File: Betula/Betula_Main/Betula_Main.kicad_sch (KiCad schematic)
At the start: 172 parts, among them J1 Conn_02x15_Top_Bottom, J2 Conn_02x02_Top_Bottom, J3 Conn_02x15_Top_Bottom, J4 Conn_01x03_Male, J5 Conn_01x03_Male, J6 Conn_02x05_Odd_Even, Q1 FDS4435BZ, Q2 DMN3030LSS, U1 PCM1803A, U10 V1402, U11 74HCT125, U12 TLV9354, U13 TLV9354, U14 TLV9352, U15 TLV9354, U16 TLV9354, U2 PCM1803A, U3 PCM1803A, U4 PCM1803A, U5 LDK320A, U6 TL062, U7 PCM1681TPWPQ1, U8 74HC4050, U9 V1401

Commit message: Added Betula v1.5.1:  Improved noise floor, 4-layer main PCB, better Panel
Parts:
- removed C29: 10uF, Capacitor_SMD:C_0805_2012Metric_Pad1.18x1.45mm_HandSolder, symbol Device:C
- removed NT1, NT2, NT3, NT4: NetTie_2, NetTie:NetTie-2_SMD_Pad2.0mm, symbol Device:NetTie_2
- added C16, C22, C28, C32: 10u, Capacitor_SMD:C_0805_2012Metric_Pad1.18x1.45mm_HandSolder, symbol Device:C
- added C68: 10uF, Capacitor_SMD:C_0805_2012Metric_Pad1.18x1.45mm_HandSolder, symbol Device:C
- C38: renamed from C33; value 10uF -> 22uF
- C39: renamed from C34; value 10uF -> 22uF
- C40: renamed from C35; value 10uF -> 22uF
- renumbered C12 to C1, C9 to C10, C7 to C11, C3 to C12, C14 to C13, C16 to C14, C1 to C15, C15 to C17, C17 to C18, C28 to C19, C26 to C20, C19 to C21, C27 to C23, C22 to C24, C18 to C25, C21 to C26, C23 to C27, C24 to C29, C13 to C3, C20 to C30, C25 to C31, C56 to C33, C30 to C34, C31 to C35, C32 to C36, C60 to C41, C61 to C42, C59 to C43, C62 to C44, C37 to C45, C36 to C46, C39 to C47, C67 to C48, C69 to C49, C11 to C5, C68 to C50, C70 to C51, C43 to C52, C42 to C53, C45 to C54, C44 to C55, C46 to C56, C47 to C57, C48 to C58, C50 to C59, C10 to C6, C49 to C60, C52 to C61, C51 to C62, C54 to C63, C53 to C64, C55 to C65, C57 to C66, C58 to C67, C64 to C69, C5 to C7, C65 to C70, C66 to C71, C63 to C72, C41 to C73, C40 to C74, C38 to C75, C6 to C9, Q2 to Q1, Q1 to Q2, R37 to R1, R56 to R10, R60 to R11, R55 to R12, R11 to R13, R13 to R14, R12 to R15, R15 to R16, R14 to R18, R16 to R19, R1 to R2, R19 to R20, R20 to R21, R18 to R22, R21 to R23, R22 to R24, R23 to R25, R25 to R26, R24 to R28, R26 to R29, R2 to R3, R29 to R30, R32 to R31, R28 to R32, R31 to R33, R30 to R34, R33 to R35, R34 to R36, R35 to R37, R36 to R38, R3 to R4, R41 to R40, R43 to R41, R44 to R42, R47 to R43, R49 to R44, R52 to R45, R45 to R46, R48 to R47, R50 to R48, R51 to R49, R38 to R5, R53 to R50, R54 to R51, R57 to R52, R58 to R53, R59 to R54, R4 to R55, R7 to R56, R6 to R57, R5 to R58, R9 to R59, R46 to R6, R8 to R60, R10 to R61, R40 to R7, R42 to R8, R61 to R9, RV5 to RV4, RV6 to RV5, RV4 to RV6, U2 to U1, U9 to U10, U1 to U2, U4 to U3, U3 to U4, U10 to U9
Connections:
- net GNDD is gone; now on net GNDA: C1.2, C14.1, C17.2, C18.1, C3.1, C30.1, C52.1, C53.1, C54.1, C55.1, C74.2, C75.1, J4.1 (Pin_1), J5.1 (Pin_1), U1.13 (DGND), U1.17 (FMT0), U1.19 (MODE0), U1.20 (MODE1), U1.9 (TEST), U10.1 (GND), U10.15 (IO0), U10.16 (IO1), U10.17 (IO2), U10.18 (IO3), U10.6 (WDCLKNEG), U11.1 (EN1), U11.10 (EN3), U11.13 (EN4), U11.4 (EN2), U11.7 (GND), U2.13 (DGND), U2.17 (FMT0), U2.19 (MODE0), U2.20 (MODE1), U2.9 (TEST), U3.13 (DGND), U3.17 (FMT0), U3.19 (MODE0), U3.20 (MODE1), U3.9 (TEST), U4.13 (DGND), U4.17 (FMT0), U4.19 (MODE0), U4.20 (MODE1), U4.9 (TEST), U7.1 (ZR1/ZR1/FMT0), U7.10 (DGND), U7.2 (*MS/ADR/FMT1), U7.3 (MC/SCL/DEMP), U7.4 (MD/SDA/MUTE), U8.11 (IN5), U8.8 (GND), U8.9 (IN4), U9.1 (GND), U9.2 (MODE0), U9.20 (HOLDERR), U9.22 (MUTE), U9.3 (CODE0), U9.4 (CODE1), U9.5 (MODE1)
- net +12V: now also C68.2
- net +3.3V: now also C16.1, C32.1
- net +5VA: now also C22.1, C28.1
- net 12V_ IN: now also PS3.1 (+VIN)
- net GNDA: now also C16.2, C22.2, C28.2, C32.2, C68.1; no longer J3.16 (Pin_16)
- no-connect marks 17 -> 18
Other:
- moved on the sheet: C10, C14, C26, C30, C38, C40, J3, PS2, PS3, U8

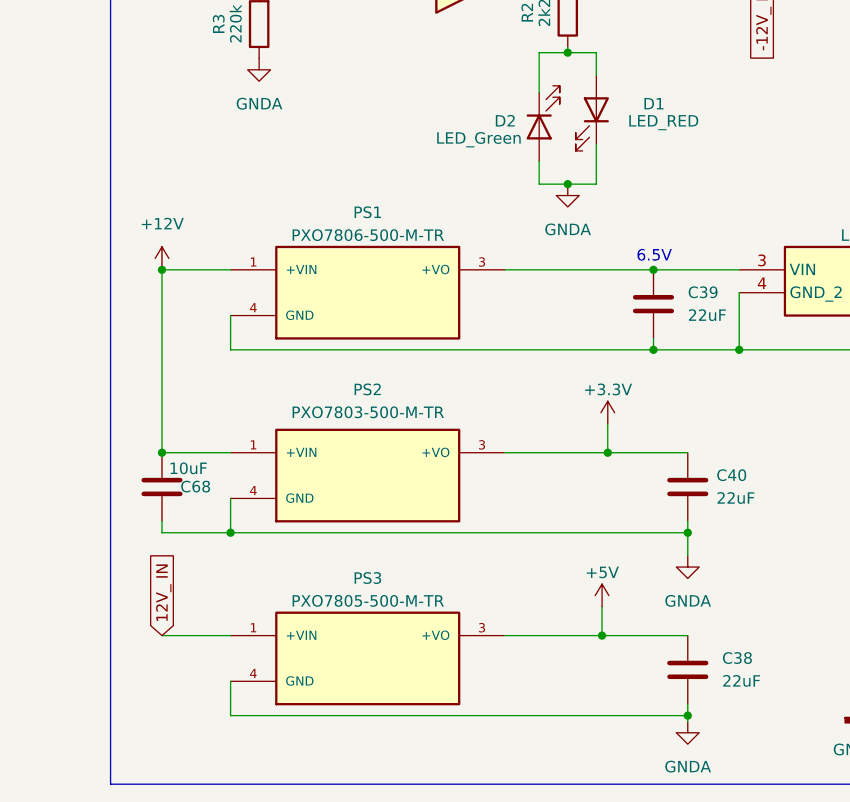
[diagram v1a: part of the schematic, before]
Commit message: Changed DC/DC converters to R-78Kx, updated to v1.5.2
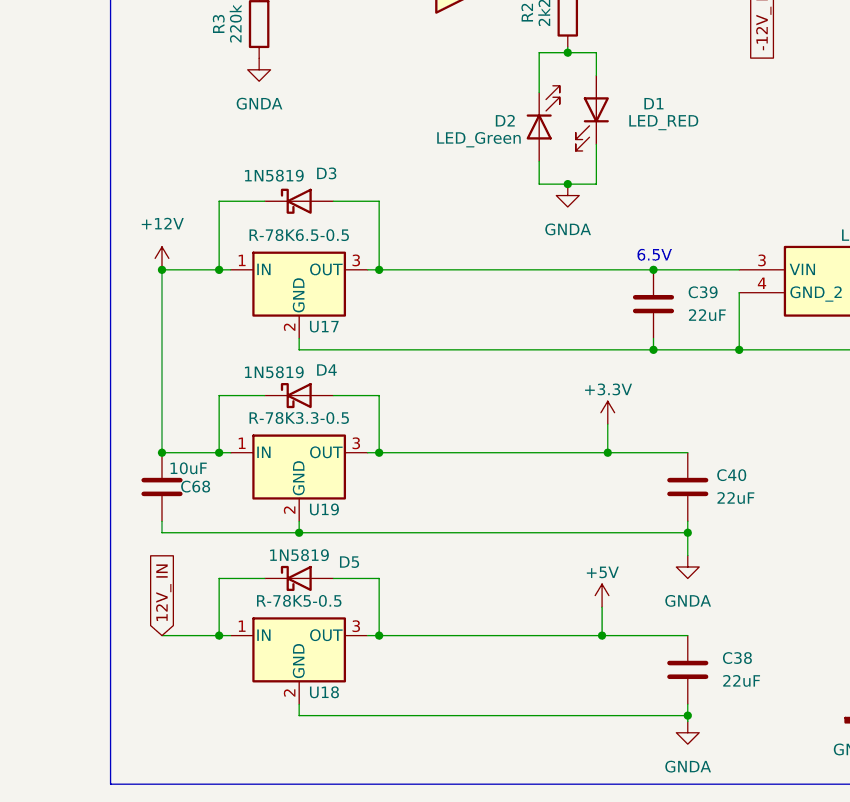
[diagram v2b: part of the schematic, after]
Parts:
- removed PS1: PXO7806-500-M-TR, Eigenes:CONV_PXO7803-500-M-TR, symbol MyLib:PXO7806-500-M-TR
- removed PS2: PXO7803-500-M-TR, Eigenes:CONV_PXO7803-500-M-TR, symbol MyLib:PXO7803-500-M-TR
- removed PS3: PXO7805-500-M-TR, Eigenes:CONV_PXO7803-500-M-TR, symbol MyLib:PXO7805-500-M-TR
- added D3, D4, D5: 1N5819, Diode_SMD:D_SOD-123, symbol Diode:1N5819
- added U17: R-78K6.5-0.5, Eigenes:Converter_DCDC_RECOM_R-78K, symbol Regulator_Switching:R-786.5-0.5
- added U18: R-78K5-0.5, Eigenes:Converter_DCDC_RECOM_R-78K, symbol Regulator_Switching:R-785.0-0.5
- added U19: R-78K3.3-0.5, Eigenes:Converter_DCDC_RECOM_R-78K, symbol Regulator_Switching:R-783.3-0.5
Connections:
- net +12V: now also D3.1 (K), D4.1 (K), U17.1 (IN), U19.1 (IN)
- net +3.3V: now also D4.2 (A), U19.3 (OUT)
- net +5V: now also D5.2 (A), U18.3 (OUT)
- net 12V_ IN: now also D5.1 (K), U18.1 (IN)
- net GNDA: now also U17.2 (GND), U18.2 (GND), U19.2 (GND)
- net at C39.2, U5.3 (VIN): now also D3.2 (A), U17.3 (OUT)
